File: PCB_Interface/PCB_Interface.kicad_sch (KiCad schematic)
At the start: 38 parts, among them J1 Conn_01x20_Socket, J2 Conn_01x20_Socket, U1 LM324, U2 LM324, U3 LM324, U4 LM324, U5 LM2662MX/NOPB, U6 LM324DT, U7 L7805, U8 L7905

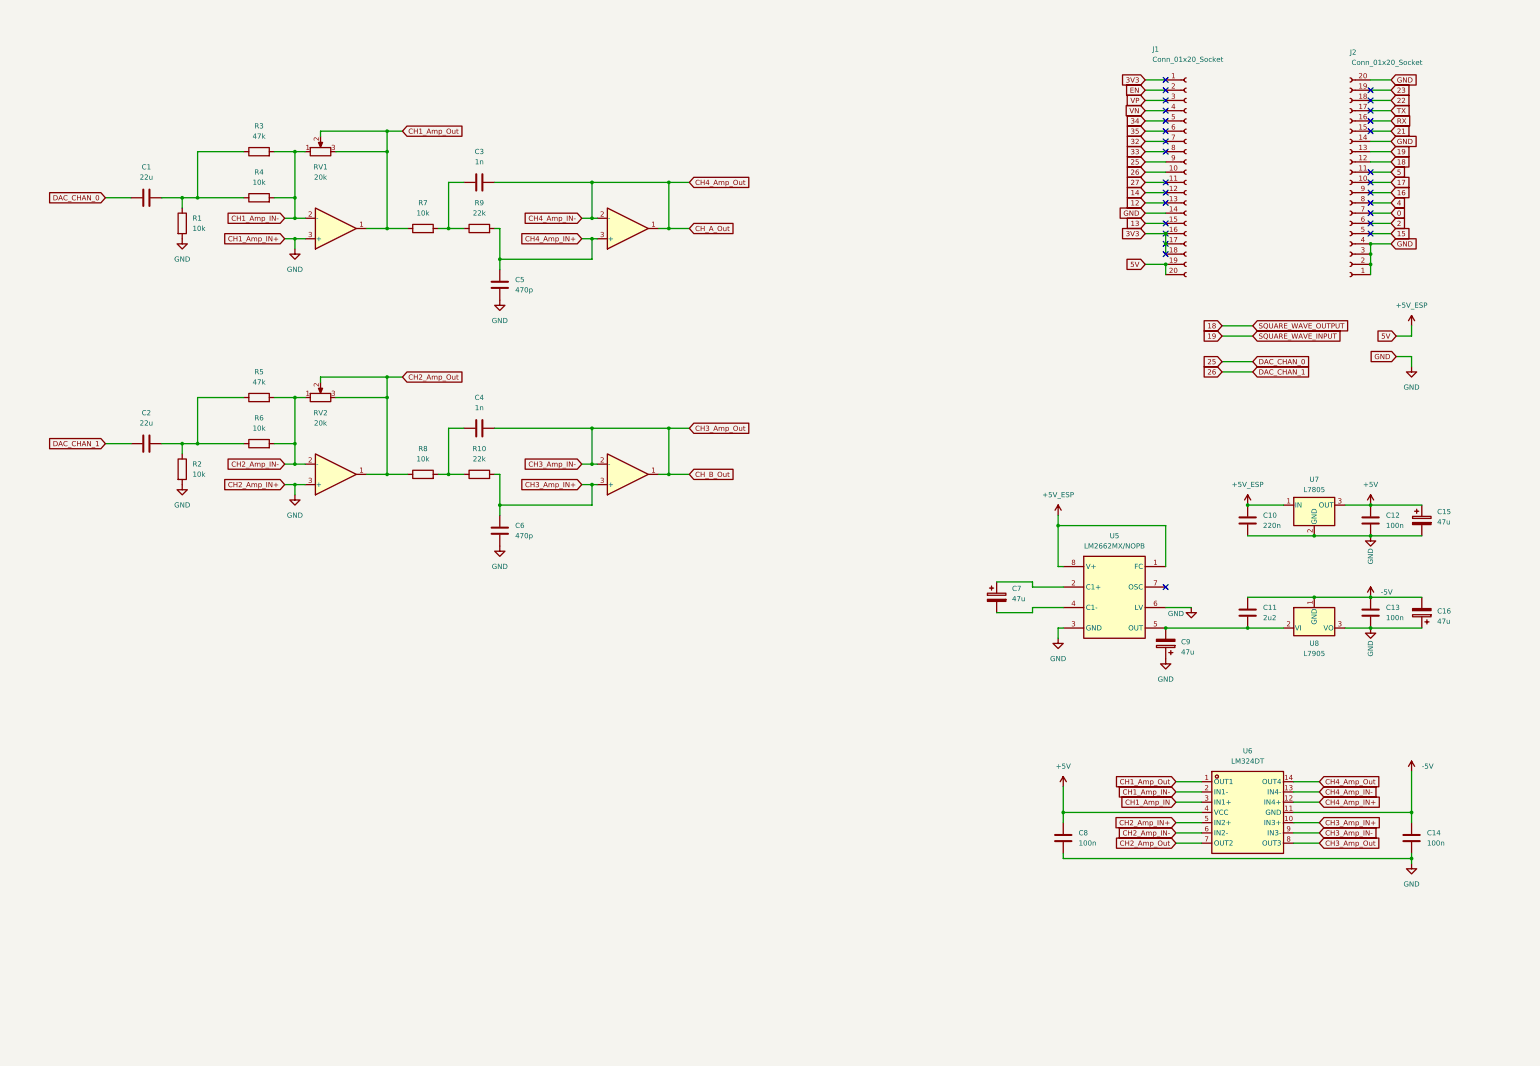
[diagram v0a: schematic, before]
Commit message: Update PCB production outputs
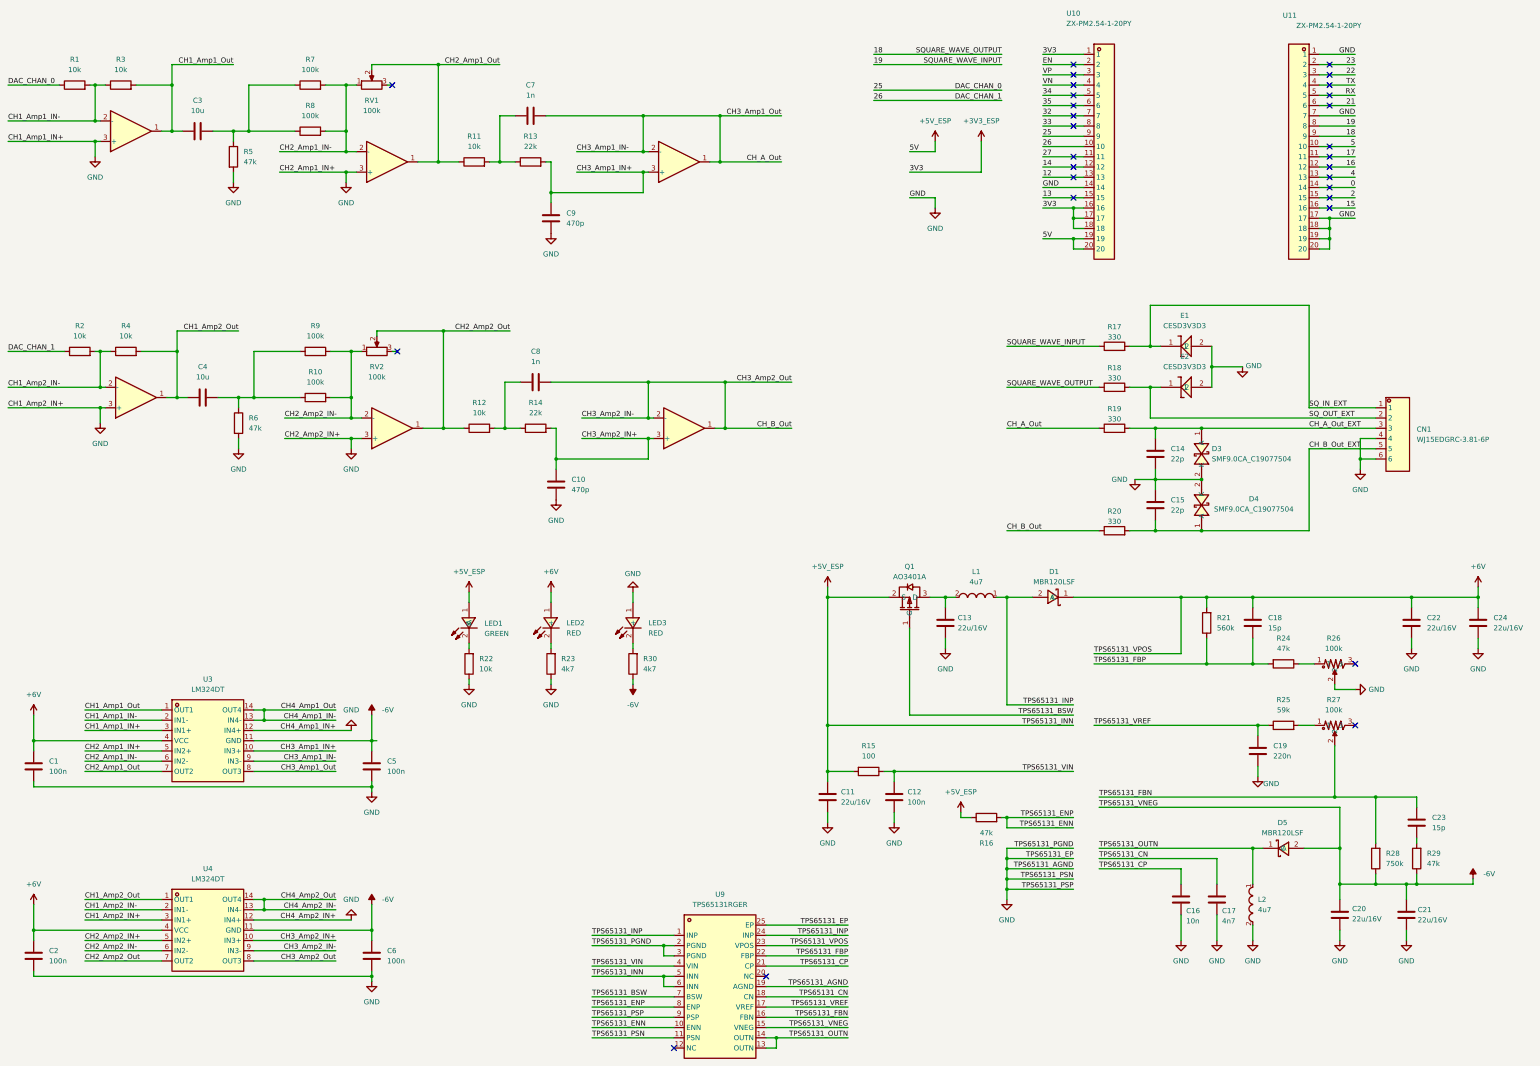
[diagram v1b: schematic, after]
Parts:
- removed C15, C16, C7, C9: 47u, Capacitor_SMD:C_0805_2012Metric, symbol Device:C_Polarized
- removed J1, J2: Conn_01x20_Socket, symbol Connector:Conn_01x20_Socket
- removed R5: 47k, Resistor_SMD:R_0603_1608Metric, symbol Device:R
- removed R8: 10k, Resistor_SMD:R_0603_1608Metric, symbol Device:R
- removed U4: LM324, symbol Amplifier_Operational:LM324
- removed U5: LM2662MX/NOPB, easyeda2kicad:SOIC-8_L4.9-W3.9-P1.27-LS6.0-BL, symbol easyeda2kicad:LM2662MX_NOPB
- removed U7: L7805, symbol Regulator_Linear:L7805
- removed U8: L7905, symbol Regulator_Linear:L7905
- added C14, C15: 22p, Capacitor_SMD:C_0603_1608Metric, symbol Device:C
- added C16: 10n, Capacitor_SMD:C_0603_1608Metric, symbol Device:C
- added C17: 4n7, Capacitor_SMD:C_0603_1608Metric, symbol Device:C
- added C18, C23: 15p, Capacitor_SMD:C_0603_1608Metric, symbol Device:C
- added C19: 220n, Capacitor_SMD:C_0603_1608Metric, symbol Device:C
- added C20, C21, C22, C24: 22u/16V, Capacitor_SMD:C_0805_2012Metric, symbol Device:C
- added C8: 1n, Capacitor_SMD:C_0603_1608Metric, symbol Device:C
- added CN1: WJ15EDGRC-3.81-6P, easyeda2kicad:CONN-TH_WJ15EDGRC-3.81-6P, symbol easyeda2kicad:WJ15EDGRC-3.81-6P
- added D1, D5: MBR120LSF, easyeda2kicad:SOD-123_L2.8-W1.8-LS3.7-RD, symbol easyeda2kicad:MBR120LSF
- added D3, D4: SMF9.0CA_C19077504, easyeda2kicad:SOD-123FL_L2.7-W1.8-LS3.8-BI, symbol easyeda2kicad:SMF9.0CA_C19077504
- added E1, E2: CESD3V3D3, :SOD-323_L1.8-W1.3-LS2.5-RD, symbol easyeda2kicad:CESD3V3D3
- added L1, L2: 4u7, easyeda2kicad:IND-SMD_L5.4-W5.2_FXL0530, symbol easyeda2kicad:FXL0530-4R7-M
- added LED1: GREEN, :LED0805-R-RD, symbol easyeda2kicad:0805G(Green)
- added LED2, LED3: RED, :LED0805-R-RD, symbol easyeda2kicad:FC-2012HRK-620D
- added Q1: AO3401A, easyeda2kicad:SOT-23_L2.9-W1.3-P1.90-LS2.4-BR, symbol easyeda2kicad:AO3401A
- added R1, R12, R22, R3, R4: 10k, Resistor_SMD:R_0603_1608Metric, symbol Device:R
- added R14: 22k, Resistor_SMD:R_0603_1608Metric, symbol Device:R
- added R15: 100, Resistor_SMD:R_0603_1608Metric, symbol Device:R
- added R16, R24, R29: 47k, Resistor_SMD:R_0603_1608Metric, symbol Device:R
- added R17, R18, R19, R20: 330, Resistor_SMD:R_0603_1608Metric, symbol Device:R
- added R21: 560k, Resistor_SMD:R_0603_1608Metric, symbol Device:R
- added R23, R30: 4k7, Resistor_SMD:R_0603_1608Metric, symbol Device:R
- added R25: 59k, Resistor_SMD:R_0603_1608Metric, symbol Device:R
- added R26, R27: 100k, easyeda2kicad:RES-ADJ-SMD_TC33X-2-104E, symbol easyeda2kicad:TC33X-2-104E
- added R28: 750k, Resistor_SMD:R_0603_1608Metric, symbol Device:R
- added R9: 100k, Resistor_SMD:R_0603_1608Metric, symbol Device:R
- added U1, U6, U8: LM324, symbol Amplifier_Operational:LM324
- added U10, U11: ZX-PM2.54-1-20PY, easyeda2kicad:HDR-TH_20P-P2.54-V-F, symbol easyeda2kicad:ZX-PM2.54-1-20PY
- added U4: LM324DT, easyeda2kicad:SOIC-14_L8.7-W3.9-P1.27-LS6.0-BL, symbol easyeda2kicad:LM324DT
- added U9: TPS65131RGER, easyeda2kicad:QFN-24_L4.0-W4.0-P0.50-TL-EP2.6, symbol easyeda2kicad:TPS65131RGER
- C1: renamed from C8; footprint Capacitor_SMD:C_0805_2012Metric -> Capacitor_SMD:C_0603_1608Metric
- C10: value 220n -> 470p; footprint Capacitor_SMD:C_0805_2012Metric -> Capacitor_SMD:C_0603_1608Metric
- C11: value 2u2 -> 22u/16V
- C12: footprint Capacitor_SMD:C_0805_2012Metric -> Capacitor_SMD:C_0603_1608Metric
- C13: value 100n -> 22u/16V
- C2: value 22u -> 100n; footprint Capacitor_SMD:C_0805_2012Metric -> Capacitor_SMD:C_0603_1608Metric
- C3: renamed from C1; value 22u -> 10u; footprint Capacitor_SMD:C_0805_2012Metric -> Capacitor_SMD:C_0603_1608Metric
- C4: value 1n -> 10u; footprint Capacitor_SMD:C_0805_2012Metric -> Capacitor_SMD:C_0603_1608Metric
- C5: renamed from C14; footprint Capacitor_SMD:C_0805_2012Metric -> Capacitor_SMD:C_0603_1608Metric
- C6: value 470p -> 100n; footprint Capacitor_SMD:C_0805_2012Metric -> Capacitor_SMD:C_0603_1608Metric
- C7: renamed from C3; footprint Capacitor_SMD:C_0805_2012Metric -> Capacitor_SMD:C_0603_1608Metric
- C9: renamed from C5; footprint Capacitor_SMD:C_0805_2012Metric -> Capacitor_SMD:C_0603_1608Metric
- R10: value 22k -> 100k
- R5: renamed from R1; value 10k -> 47k
- R6: value 10k -> 47k
- R7: renamed from R3; value 47k -> 100k
- R8: renamed from R4; value 10k -> 100k
- RV1, RV2: value 20k -> 100k; footprint (none) -> easyeda2kicad:RES-ADJ-TH_3296P; LCSC Part (none) -> C780112
- renumbered R7 to R11, R9 to R13, U6 to U3, U1 to U5, U3 to U7
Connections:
- net CH1_Amp_IN is gone; now on net GND: U3.3 (IN1+)
- net +5V_ESP: now also C11.1, LED1.1 (A), Q1.2 (S), R15.2, R16.1, U10.19, U10.20, U9.5 (INN), U9.6 (INN); no longer C10.1
- net 0: now also U11.14
- net 12: now also U10.13
- net 13: now also U10.15
- net 14: now also U10.12
- net 15: now also U11.16
- net 16: now also U11.12
- net 17: now also U11.11
- net 18: now also R18.1, U11.9
- net 19: now also R17.1, U11.8
- net 2: now also U11.15
- net 21: now also U11.6
- net 22: now also U11.3
- net 23: now also U11.2
- net 25: now also R1.1, U10.9; no longer C3.1
- net 26: now also R2.1, U10.10; no longer C2.1
- net 27: now also U10.11
- net 32: now also U10.7
- net 33: now also U10.8
- net 34: now also U10.5
- net 35: now also U10.6
- net 4: now also U11.13
- net 5: now also U11.10
- net EN: now also U10.2
- net GND: now also C10.1, C11.2, C2.1, R6.2, U3.12 (IN4+), C14.2, C15.1, C16.2, C17.2, C19.2, C20.2, C21.2, C22.2, C24.2, CN1.4, CN1.6, D3.2 (K), D4.2 (K), E1.2, E2.2, L2.2, LED3.1 (+), R22.1, R23.1, R26.2, U1.3 (+), U10.14, U11.1, U11.17, U11.18, U11.19, U11.20, U11.7, U4.12 (IN4+), U4.3 (IN1+), U4.5 (IN2+), U6.3 (+), U9.11 (PSN), U9.19 (AGND), U9.2 (PGND), U9.25 (EP), U9.3 (PGND), U9.9 (PSP); no longer C10.2, R2.2
- net RX: now also U11.5
- net TX: now also U11.4
- net VN: now also U10.4
- net VP: now also U10.3
- net at R10.1: now also C4.2, R6.1, R9.1; no longer C4.1
- net +5V renamed +6V
- net +6V: now also C2.2, C18.1, C22.1, C24.1, D1.1 (C), LED2.1 (+), R21.2, U4.4 (VCC), U9.23 (VPOS); no longer C12.1
- net -5V renamed -6V
- net -6V: now also C6.2, C20.1, C21.1, D5.2 (A), R28.1, R29.1, R30.1, U4.11 (GND), U9.15 (VNEG); no longer C11.1, C13.1
- net CH1_Amp_IN- renamed CH2_Amp1_IN-
- net CH2_Amp1_IN-: now also U3.6 (IN2-); no longer U3.2 (IN1-)
- net CH1_Amp_Out renamed CH2_Amp1_Out
- net CH2_Amp1_Out: now also U3.7 (OUT2); no longer RV1.3, U3.1 (OUT1)
- removed net CH2_Amp_IN-: R6.2, RV2.1, U2.2 (-), U3.6 (IN2-)
- removed net CH2_Amp_Out: RV2.2, RV2.3, U2.1, U3.7 (OUT2)
- removed net CH3_Amp_IN+: C6.2, R10.2, U3.10 (IN3+)
- net CH3_Amp_IN- renamed CH3_Amp1_IN-
- net CH3_Amp1_IN-: now also C7.2, U7.1, U7.2 (-), R19.1; no longer C4.2
- net CH4_Amp_IN+ renamed CH3_Amp1_IN+
- net CH3_Amp1_IN+: now also U3.10 (IN3+); no longer U3.12 (IN4+)
- removed net CH4_Amp_IN-: C7.2, U3.13 (IN4-), U3.14 (OUT4), U7.1, U7.2 (-)
- new net: LED3.2 (-), R30.2
- new net: C13.1, L1.2, Q1.3 (D)
- new net: LED1.2 (K), R22.2
- new net: LED2.2 (-), R23.2
- new net: C23.2, R29.2
- new net: R25.2, R27.1
- new net: C8.1, R12.2, R14.1
- new net: R24.1, R26.1
- new net +3V3_ESP: U10.1, U10.16, U10.17, U10.18
- new net CH1_Amp1_IN-: R1.2, R3.1, U1.2 (-), U3.2 (IN1-)
- new net CH1_Amp1_Out: C3.1, R3.2, U1.1, U3.1 (OUT1)
- new net CH1_Amp2_IN-: R2.2, R4.1, U2.2 (-), U4.2 (IN1-)
- new net CH1_Amp2_Out: C4.1, R4.2, U2.1, U4.1 (OUT1)
- new net CH2_Amp2_IN-: R10.2, R9.2, RV2.1, U4.6 (IN2-), U6.2 (-)
- new net CH2_Amp2_Out: R12.1, RV2.2, U4.7 (OUT2), U6.1
- new net CH3_Amp2_IN+: C10.2, R14.2, U4.10 (IN3+), U8.3 (+)
- new net CH3_Amp2_IN-: C8.2, R20.1, U4.8 (OUT3), U4.9 (IN3-), U8.1, U8.2 (-)
- new net CH4_Amp1_IN-: U3.13 (IN4-), U3.14 (OUT4)
- new net CH4_Amp2_IN-: U4.13 (IN4-), U4.14 (OUT4)
- new net CH_A_Out_EXT: C14.1, CN1.3, D3.1 (A), R19.2
- new net CH_B_Out_EXT: C15.2, CN1.5, D4.1 (A), R20.2
- new net SQ_IN_EXT: CN1.1, E1.1, R17.2
- new net SQ_OUT_EXT: CN1.2, E2.1, R18.2
- new net TPS65131_BSW: Q1.1 (G), U9.7 (BSW)
- new net TPS65131_CN: C17.1, U9.18 (CN)
- new net TPS65131_CP: C16.1, U9.21 (CP)
- new net TPS65131_ENN: R16.2, U9.10 (ENN), U9.8 (ENP)
- new net TPS65131_FBN: C23.1, R27.2, R28.2, U9.16 (FBN)
- new net TPS65131_FBP: C18.2, R21.1, R24.2, U9.22 (FBP)
- new net TPS65131_INP: D1.2 (A), L1.1, U9.1 (INP), U9.24 (INP)
- new net TPS65131_OUTN: D5.1 (C), L2.1, U9.13 (OUTN), U9.14 (OUTN)
- new net TPS65131_VIN: C12.1, R15.1, U9.4 (VIN)
- new net TPS65131_VREF: C19.1, R25.1, U9.17 (VREF)
- no-connect marks 28 -> 29
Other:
- moved on the sheet: C1, C3, C5, C7, C9, R11, R13, R5, R7, R8, RV1, U3
